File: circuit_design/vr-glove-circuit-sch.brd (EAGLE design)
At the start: 100 x 80 mm, 31 parts, among them U1 ARDUINO_SHIELDNO_SILK

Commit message: saved
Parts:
- moved R7 3.59 mm to (44.5, 17.8)
- moved U$1 2.54 mm to (31.8, 27.9)
- moved U$3 2.54 mm to (62.2, 55.9)
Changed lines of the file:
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@@
 <element name="R4" library="SparkFun-Resistors" package="AXIAL-0.5" value="" x="77.47" y="6.35" rot="R180"/>
 <element name="R5" library="SparkFun-Resistors" package="AXIAL-0.5" value="" x="49.53" y="36.83" rot="R180"/>
-<element name="R7" library="SparkFun-Resistors" package="AXIAL-0.5" value="" x="46.99" y="20.32" rot="MR0"/>
-<element name="U$1" library="GeekAmmo" package="SOT23-3" value="N-CHANNEL-MOSFET-BSS138" x="34.29" y="27.94">
-<attribute name="DATASHEET" value="http://www.fairchildsemi.com/ds/BS/BSS138.pdf" x="34.29" y="27.94" size="1.778" layer="27" display="off"/>
-<attribute name="URL" value="http://au.element14.com/fairchild-semiconductor/bss138/mosfet-n-ch-50v-220ma-sot-23/dp/2323154" x="34.29" y="27.94" size="1.778" layer="27" display="off"/>
-<attribute name="ELEMENT14" value="2323154" x="34.29" y="27.94" size="1.778" layer="27" display="off"/>
-<attribute name="OTHER" value="" x="34.29" y="27.94" size="1.778" layer="27" display="off"/>
-<attribute name="DIGIKEY" value="BSS138TR-ND" x="34.29" y="27.94" size="1.778" layer="27" display="off"/>
+<element name="R7" library="SparkFun-Resistors" package="AXIAL-0.5" value="" x="44.45" y="17.78" rot="MR0"/>
+<element name="U$1" library="GeekAmmo" package="SOT23-3" value="N-CHANNEL-MOSFET-BSS138" x="31.75" y="27.94">
+<attribute name="DATASHEET" value="http://www.fairchildsemi.com/ds/BS/BSS138.pdf" x="31.75" y="27.94" size="1.778" layer="27" display="off"/>
+<attribute name="URL" value="http://au.element14.com/fairchild-semiconductor/bss138/mosfet-n-ch-50v-220ma-sot-23/dp/2323154" x="31.75" y="27.94" size="1.778" layer="27" display="off"/>
+<attribute name="ELEMENT14" value="2323154" x="31.75" y="27.94" size="1.778" layer="27" display="off"/>
+<attribute name="OTHER" value="" x="31.75" y="27.94" size="1.778" layer="27" display="off"/>
+<attribute name="DIGIKEY" value="BSS138TR-ND" x="31.75" y="27.94" size="1.778" layer="27" display="off"/>
 </element>
 <element name="U$2" library="GeekAmmo" package="SOT23-3" value="N-CHANNEL-MOSFET-BSS138" x="33.02" y="16.51" rot="R90">
@@
 <attribute name="DIGIKEY" value="BSS138TR-ND" x="33.02" y="16.51" size="1.778" layer="27" rot="R90" display="off"/>
 </element>
-<element name="U$3" library="GeekAmmo" package="SOT23-3" value="N-CHANNEL-MOSFET-BSS138" x="59.69" y="55.88" rot="R180">
-<attribute name="DATASHEET" value="http://www.fairchildsemi.com/ds/BS/BSS138.pdf" x="59.69" y="55.88" size="1.778" layer="27" rot="R180" display="off"/>
-<attribute name="URL" value="http://au.element14.com/fairchild-semiconductor/bss138/mosfet-n-ch-50v-220ma-sot-23/dp/2323154" x="59.69" y="55.88" size="1.778" layer="27" rot="R180" display="off"/>
-<attribute name="ELEMENT14" value="2323154" x="59.69" y="55.88" size="1.778" layer="27" rot="R180" display="off"/>
-<attribute name="OTHER" value="" x="59.69" y="55.88" size="1.778" layer="27" rot="R180" display="off"/>
-<attribute name="DIGIKEY" value="BSS138TR-ND" x="59.69" y="55.88" size="1.778" layer="27" rot="R180" display="off"/>
+<element name="U$3" library="GeekAmmo" package="SOT23-3" value="N-CHANNEL-MOSFET-BSS138" x="62.23" y="55.88" rot="R180">
+<attribute name="DATASHEET" value="http://www.fairchildsemi.com/ds/BS/BSS138.pdf" x="62.23" y="55.88" size="1.778" layer="27" rot="R180" display="off"/>
+<attribute name="URL" value="http://au.element14.com/fairchild-semiconductor/bss138/mosfet-n-ch-50v-220ma-sot-23/dp/2323154" x="62.23" y="55.88" size="1.778" layer="27" rot="R180" display="off"/>
+<attribute name="ELEMENT14" value="2323154" x="62.23" y="55.88" size="1.778" layer="27" rot="R180" display="off"/>
+<attribute name="OTHER" value="" x="62.23" y="55.88" size="1.778" layer="27" rot="R180" display="off"/>
+<attribute name="DIGIKEY" value="BSS138TR-ND" x="62.23" y="55.88" size="1.778" layer="27" rot="R180" display="off"/>
 </element>
 <element name="U$4" library="GeekAmmo" package="SOT23-3" value="N-CHANNEL-MOSFET-BSS138" x="24.13" y="12.7" rot="R180">
@@
 <contactref element="R7" pad="P$2"/>
 <contactref element="U$1" pad="1"/>
-<wire x1="33.34" y1="26.94" x2="40.64" y2="20.32" width="0" layer="19" extent="1-1"/>
+<wire x1="30.8" y1="26.94" x2="38.1" y2="17.78" width="0" layer="19" extent="1-1"/>
 </signal>
 <signal name="N$2">
@@
 <contactref element="JP10" pad="2"/>
 <wire x1="64.77" y1="39.76" x2="73.66" y2="44.45" width="0" layer="19" extent="1-1"/>
-<wire x1="35.24" y1="26.94" x2="64.77" y2="39.76" width="0" layer="19" extent="1-1"/>
-<wire x1="17.78" y1="27.94" x2="35.24" y2="26.94" width="0" layer="19" extent="1-1"/>
+<wire x1="32.7" y1="26.94" x2="64.77" y2="39.76" width="0" layer="19" extent="1-1"/>
+<wire x1="17.78" y1="27.94" x2="32.7" y2="26.94" width="0" layer="19" extent="1-1"/>
 </signal>
 <signal name="N$4">
@@
 <contactref element="R2" pad="P$2"/>
 <contactref element="U$3" pad="1"/>
-<wire x1="60.64" y1="56.88" x2="80.01" y2="45.72" width="0" layer="19" extent="1-1"/>
+<wire x1="63.18" y1="56.88" x2="80.01" y2="45.72" width="0" layer="19" extent="1-1"/>
 </signal>
 <signal name="N$8">
@@
 <contactref element="U$3" pad="2"/>
 <contactref element="JP11" pad="4"/>
-<wire x1="50.8" y1="67.31" x2="58.74" y2="56.88" width="0" layer="19" extent="1-1"/>
+<wire x1="50.8" y1="67.31" x2="61.28" y2="56.88" width="0" layer="19" extent="1-1"/>
 <wire x1="34.29" y1="69.46" x2="50.8" y2="67.31" width="0" layer="19" extent="1-1"/>
 <wire x1="17.78" y1="48.26" x2="34.29" y2="69.46" width="0" layer="19" extent="1-1"/>
@@
 <contactref element="R7" pad="P$1"/>
 <contactref element="U1" pad="D3"/>
-<wire x1="58.42" y1="24.13" x2="53.34" y2="20.32" width="0" layer="19" extent="1-1"/>
+<wire x1="58.42" y1="24.13" x2="50.8" y2="17.78" width="0" layer="19" extent="1-1"/>
 </signal>
 <signal name="N$20">
@@
 <contactref element="U$6" pad="3"/>
 <contactref element="JP2" pad="2"/>
-<wire x1="72.12" y1="36.83" x2="59.69" y2="54.88" width="0" layer="19" extent="1-1"/>
+<wire x1="72.12" y1="36.83" x2="62.23" y2="54.88" width="0" layer="19" extent="1-1"/>
 <wire x1="87.63" y1="24.13" x2="72.12" y2="36.83" width="0" layer="19" extent="1-1"/>
-<wire x1="36.83" y1="47.26" x2="59.69" y2="54.88" width="0" layer="19" extent="1-1"/>
-<wire x1="34.29" y1="28.94" x2="36.83" y2="47.26" width="0" layer="19" extent="1-1"/>
-<wire x1="32.02" y1="16.51" x2="34.29" y2="28.94" width="0" layer="19" extent="1-1"/>
+<wire x1="36.83" y1="47.26" x2="62.23" y2="54.88" width="0" layer="19" extent="1-1"/>
+<wire x1="31.75" y1="28.94" x2="36.83" y2="47.26" width="0" layer="19" extent="1-1"/>
+<wire x1="32.02" y1="16.51" x2="31.75" y2="28.94" width="0" layer="19" extent="1-1"/>
 <wire x1="24.13" y1="11.7" x2="32.02" y2="16.51" width="0" layer="19" extent="1-1"/>
 <wire x1="96.647" y1="15.24" x2="24.13" y2="11.7" width="0" layer="19" extent="1-1"/>

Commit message: added power supply
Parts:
- added C8: (no value), SparkFun-Capacitors:0402-CAP
- added D8: BA340A, SparkFun-DiscreteSemi:SMA-DIODE
- added U2: (no value), SparkFun-PowerIC:78XXL
- C7: device SparkFun-Capacitors:CAP-PTH-SMALL -> SparkFun-Capacitors:0402-CAP
- moved C7 56.2 mm to (22.9, 68.6), turned to 270 degrees
- moved JP11 11.4 mm to (7.62, 35.6)
- moved JP10 2.54 mm to (15.2, 25.4)
- moved D7 2.54 mm to (64.8, 39.4)
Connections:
- new net N$25: C7.2, D8.C, U2.IN
- new net N$9: D8.A, JP1.VIN0
- net GND: now also C7.1, C8.1, U2.GND; no longer C7.2
- net VCC: now also C8.2, U2.OUT; no longer C7.1, JP1.VIN0
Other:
- board size 100 x 80 mm -> 100 x 82.5 mm

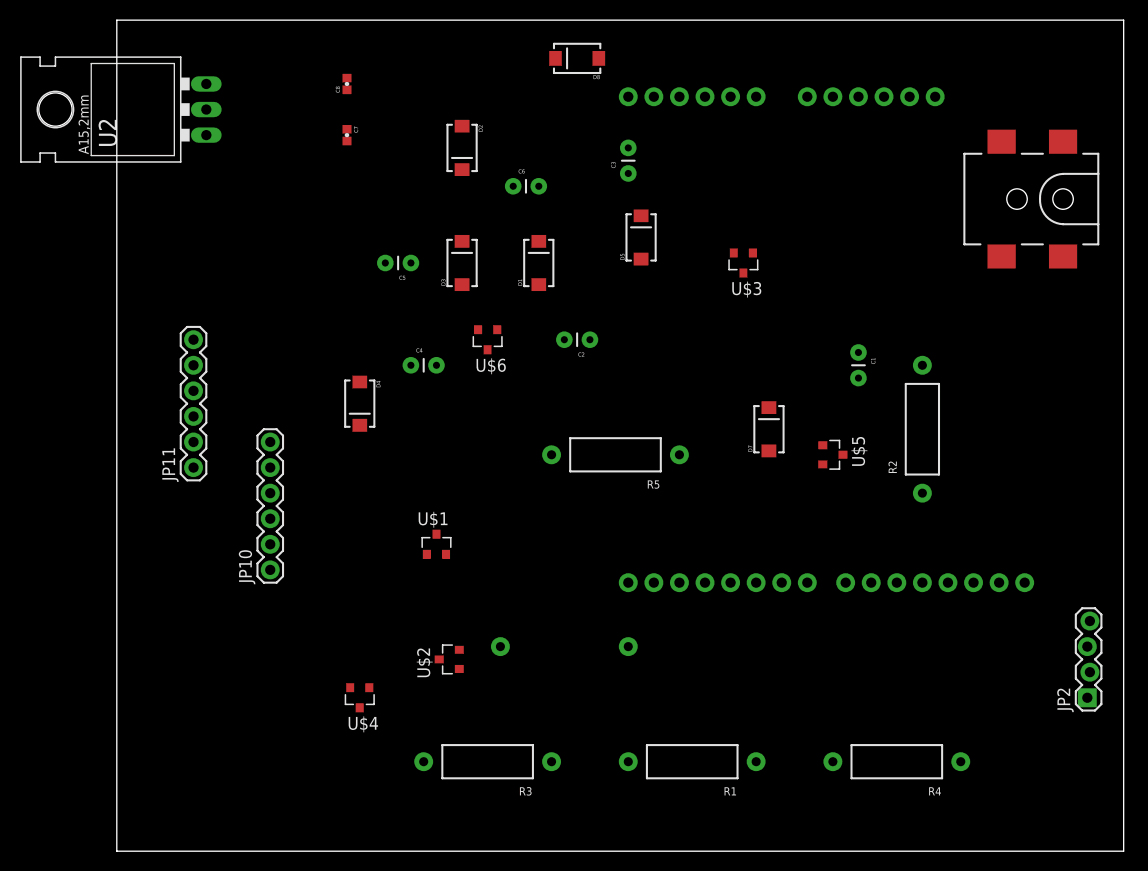
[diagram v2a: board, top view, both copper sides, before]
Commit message: finished initial design for schematic and board. still need to complete silkscreen labels and testing.
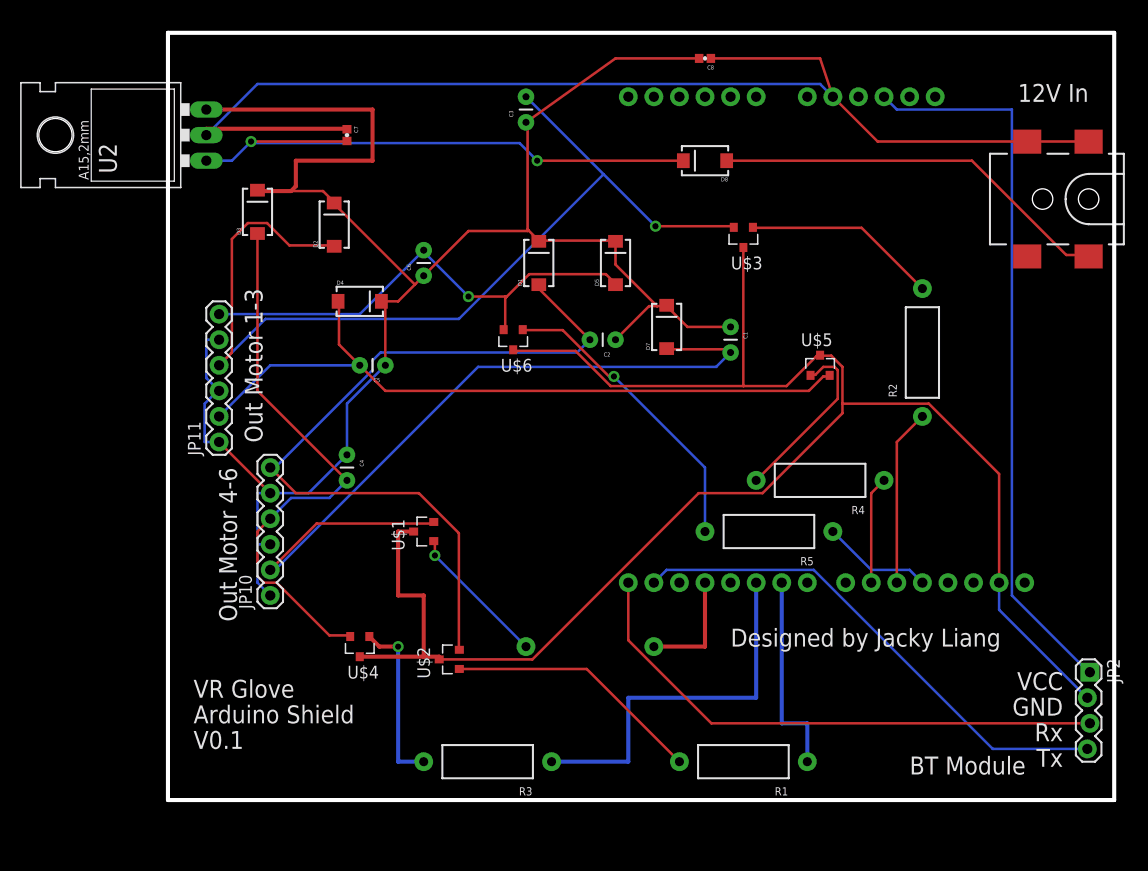
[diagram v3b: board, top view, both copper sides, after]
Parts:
- moved C8 35.7 mm to (58.4, 76.2), turned to 180 degrees
- moved R4 29.0 mm to (69.8, 34.3)
- moved D3 20.9 mm to (14.0, 61.0)
- moved R5 17.0 mm to (64.8, 29.2)
- moved D8 16.3 mm to (58.4, 66.0)
- moved D2 14.8 mm to (21.6, 59.7), turned to 90 degrees
- moved D7 14.4 mm to (54.6, 49.5)
- moved C1 13.0 mm to (61.0, 49.5)
- moved C6 12.6 mm to (30.5, 54.6), turned to 90 degrees
- moved C3 11.4 mm to (40.6, 69.8)
- moved C4 10.9 mm to (22.9, 36.8), turned to 270 degrees
- moved C5 10.5 mm to (26.7, 45.7)
- moved D4 10.2 mm to (24.1, 52.1), turned to 0 degrees
- moved U$5 8.98 mm to (69.8, 45.7), turned to 0 degrees
- moved R2 7.62 mm to (80.0, 47.0)
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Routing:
- net VCC: track 0.00 -> 194.8 mm
- net N$3: track 0.00 -> 173.7 mm
- net GND: track 0.00 -> 121.6 mm
- net N$8: track 0.00 -> 97.0 mm, vias 0 -> 1
- net N$2: track 0.00 -> 79.5 mm
- net N$5: track 0.00 -> 78.2 mm
- net N$6: track 0.00 -> 72.4 mm
- net N$14: track 0.00 -> 71.7 mm
- net N$25: track 0.00 -> 58.6 mm, vias 0 -> 2
- net N$11: track 0.00 -> 55.4 mm
- net N$12: track 0.00 -> 55.0 mm
- net N$15: track 0.00 -> 50.9 mm
- net N$17: track 0.00 -> 48.8 mm, vias 0 -> 1
- net N$9: track 0.00 -> 40.0 mm
- net N$20: track 0.00 -> 38.1 mm
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- added copper zone on layer 1, net GND
- added copper zone on layer 16, net GND
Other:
- board size 100 x 82.5 mm -> 94 x 76.2 mm
- board text added: "12V In"
- board text added: "Arduino Shield"
- board text added: "BT Module"
- board text added: "Designed by Jacky Liang"
- board text added: "GND"
- board text added: "Out Motor 1-3"
- board text added: "Out Motor 4-6"
- board text added: "Rx"
- board text added: "Tx"
- board text added: "V0.1"
- board text added: "VCC"
- board text added: "VR Glove"

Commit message: finialized circuit design
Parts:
- renumbered U$1 to T1, U$2 to T2, U$3 to T3, U$4 to T4, U$5 to T5, U$6 to T6

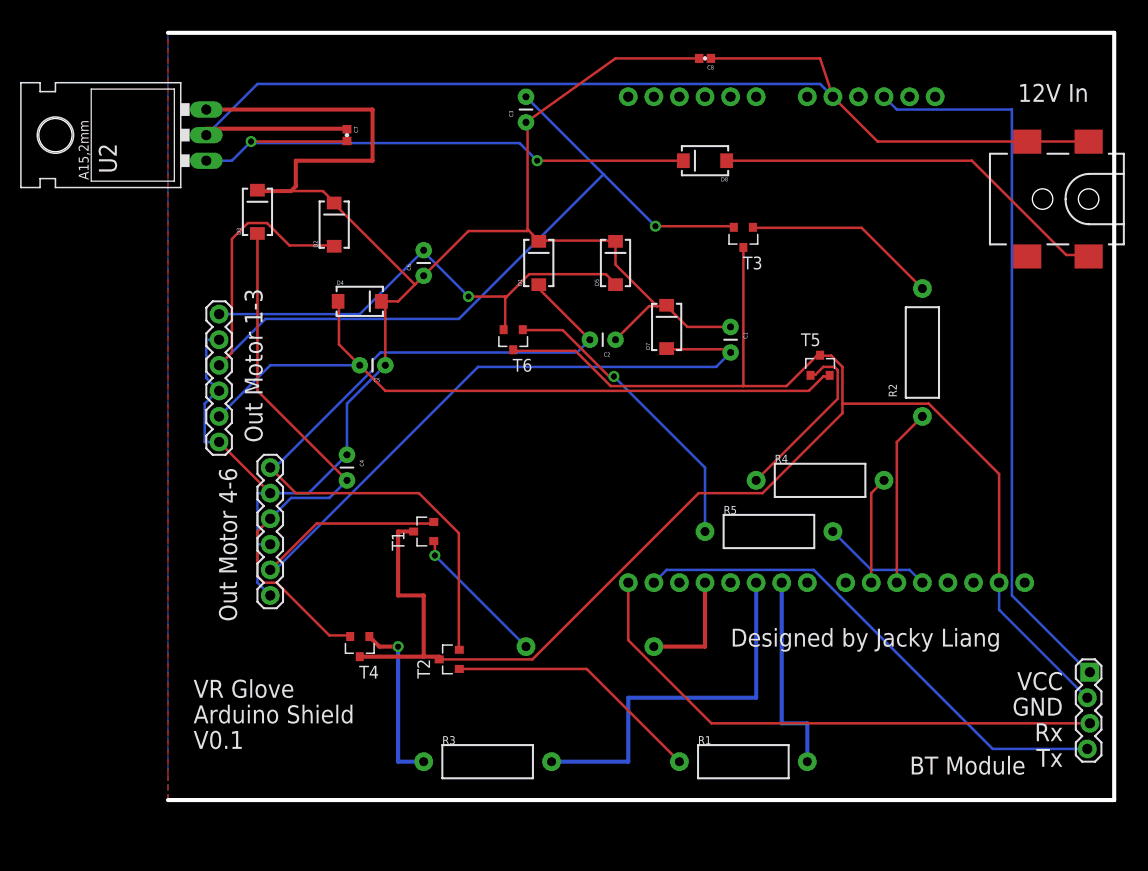
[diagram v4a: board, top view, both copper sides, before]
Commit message: working wireless communication
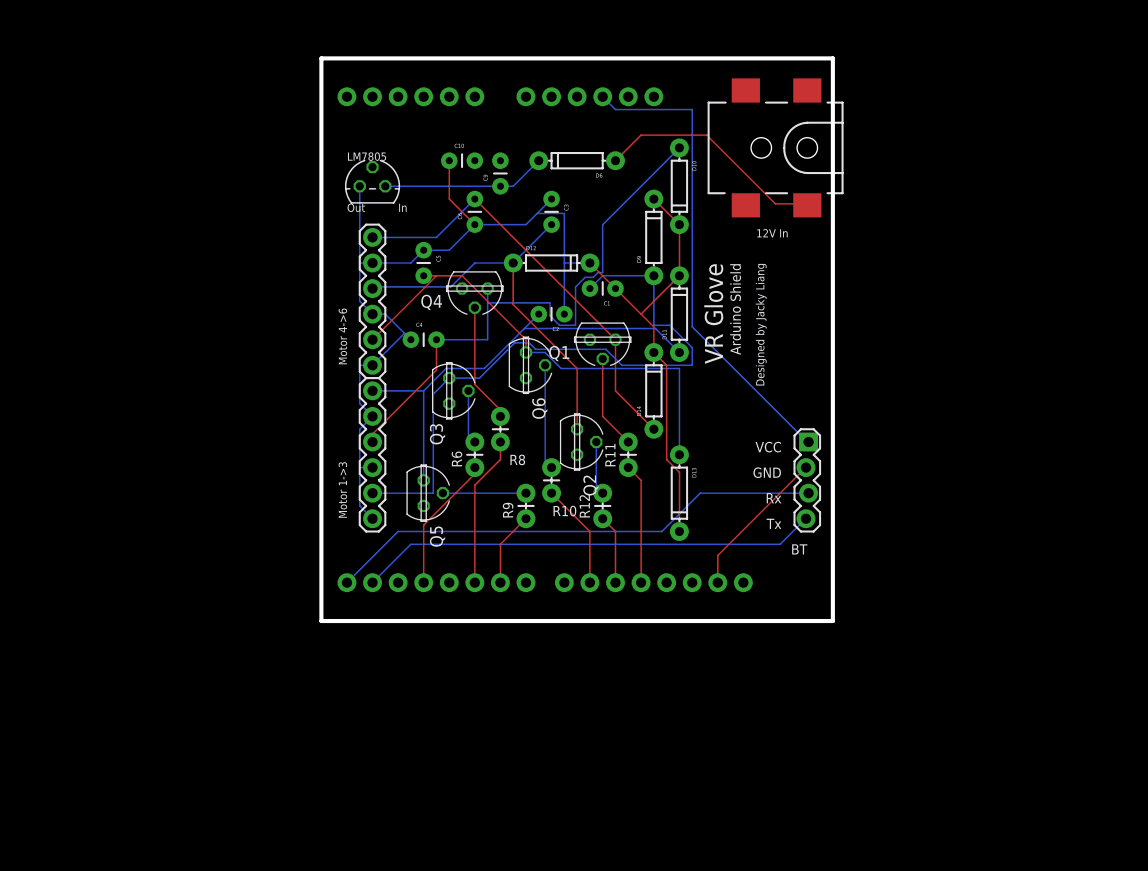
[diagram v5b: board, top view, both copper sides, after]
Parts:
- removed C7, C8: (no value), SparkFun-Capacitors:0402-CAP
- removed D1, D2, D3, D4, D5, D7: (no value), SparkFun-DiscreteSemi:SMA-DIODE
- removed D8: BA340A, SparkFun-DiscreteSemi:SMA-DIODE
- removed FRAME1: (no value), SparkFun-Aesthetics:CREATIVE_COMMONS
- removed R1, R2, R3, R4, R5, R7: (no value), SparkFun-Resistors:AXIAL-0.5
- removed T1, T2, T3, T4, T5, T6: N-CHANNEL-MOSFET-BSS138, GeekAmmo:SOT23-3
- removed U2: (no value), SparkFun-PowerIC:78XXL
- added C10, C9: (no value), SparkFun-Passives:CAP-PTH-SMALL
- added D10, D11, D12, D13, D14, D6, D9: (no value), SparkFun-DiscreteSemi:DIODE-1N4148
- added IC2: 7818L, linear:TO92
- added Q1, Q2, Q3, Q4, Q5, Q6: VN2222KM, transistor-fet:TO237
- added R10, R11, R12, R6, R8, R9: (no value), SparkFun-Resistors:AXIAL-0.1
- moved JP2 36.1 mm to (68.6, 38.1)
- moved JP1 28.4 mm to (68.6, 67.3)
- moved U1 27.9 mm to (64.8, 21.6)
- moved JP11 17.0 mm to (25.4, 45.7)
- moved C4 13.1 mm to (29.2, 48.3), turned to 0 degrees
- moved JP10 12.7 mm to (25.4, 30.5)
- moved C1 12.0 mm to (49.5, 53.3), turned to 180 degrees
- moved C5 12.0 mm to (30.5, 57.1), turned to 270 degrees
- moved C3 8.03 mm to (43.2, 62.2), turned to 270 degrees
- moved C6 7.18 mm to (35.6, 59.7)
- moved C2 5.68 mm to (44.5, 50.8)
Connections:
- removed net N$25: C7.2, D8.C, U2.IN
- new net N$18: C9.1, D6.C, IC2.3
- net GND: now also C10.2, C9.2, IC2.2, Q1.1, Q2.1, Q3.1, Q4.1, Q5.1, Q6.1; no longer C7.1, C8.1, U2.GND
- net N$1: now also Q3.2, R6.P$2; no longer R7.P$2, T1.1
- net N$10: now also Q4.2, R8.P$2; no longer R3.P$2, T4.1
- net N$11: now also D10.A, Q4.3; no longer D3.A, T4.2
- net N$13: now also Q6.2, R10.P$2; no longer R4.P$2, T5.1
- net N$14: now also D13.A, Q6.3; no longer D4.A, T5.2
- net N$16: now also Q1.2, R11.P$2; no longer R5.P$2, T6.1
- net N$17: now also D14.A, Q1.3; no longer D5.A, T6.2
- net N$19: now also R6.P$1; no longer R7.P$1
- net N$2: now also D9.A, Q3.3; no longer D7.A, T1.2
- net N$20: now also R8.P$1; no longer R3.P$1
- net N$21: now also R9.P$1; no longer R1.P$1
- net N$22: now also R10.P$1; no longer R4.P$1
- net N$23: now also R12.P$1; no longer R2.P$1
- net N$24: now also R11.P$1; no longer R5.P$1
- net N$3: no longer T1.3, T2.3, T3.3, T4.3, T5.3, T6.3
- net N$4: now also Q5.2, R9.P$2; no longer R1.P$2, T2.1
- net N$5: now also D11.A, Q5.3; no longer D1.A, T2.2
- net N$7: now also Q2.2, R12.P$2; no longer R2.P$2, T3.1
- net N$8: now also D12.A, Q2.3; no longer D2.A, T3.2
- net N$9: now also D6.A; no longer D8.A
- net VCC: now also C10.1, D10.C, D11.C, D12.C, D13.C, D14.C, D9.C, IC2.1; no longer C8.2, D1.C, D2.C, D3.C, D4.C, D5.C, D7.C, U2.OUT
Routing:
- net N$3: track 173.7 -> 15.1 mm
- net GND: track 121.6 -> 0.00 mm
- net VCC: track 194.8 -> 130.9 mm
- net N$25: track 58.6 -> 0.00 mm, vias 2 -> 0
- net N$8: track 97.0 -> 39.6 mm, vias 1 -> 0
- net N$5: track 78.2 -> 44.9 mm
- net N$6: track 72.4 -> 47.3 mm
- net N$14: track 71.7 -> 47.5 mm
- net N$20: track 38.1 -> 15.0 mm
- net N$16: track 30.2 -> 9.31 mm, vias 1 -> 0
- net N$4: track 25.7 -> 8.26 mm
- net N$9: track 40.0 -> 23.1 mm
- net N$2: track 79.5 -> 62.9 mm
- net N$18: track 0.00 -> 16.3 mm
- net N$7: track 19.4 -> 5.71 mm
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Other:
- board size 94 x 76.2 mm -> 50.8 x 55.9 mm
- board text added: "BT"
- board text added: "In"
- board text added: "LM7805"
- board text added: "Motor 1->3"
- board text added: "Motor 4->6"
- board text added: "Out"
- board text removed: "BT Module"
- board text removed: "Out Motor 1-3"
- board text removed: "Out Motor 4-6"
- board text removed: "V0.1"
